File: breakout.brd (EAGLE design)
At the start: 25.4 x 32.4 mm, 20 parts, among them IC2 REG1117, Y1 12mhz

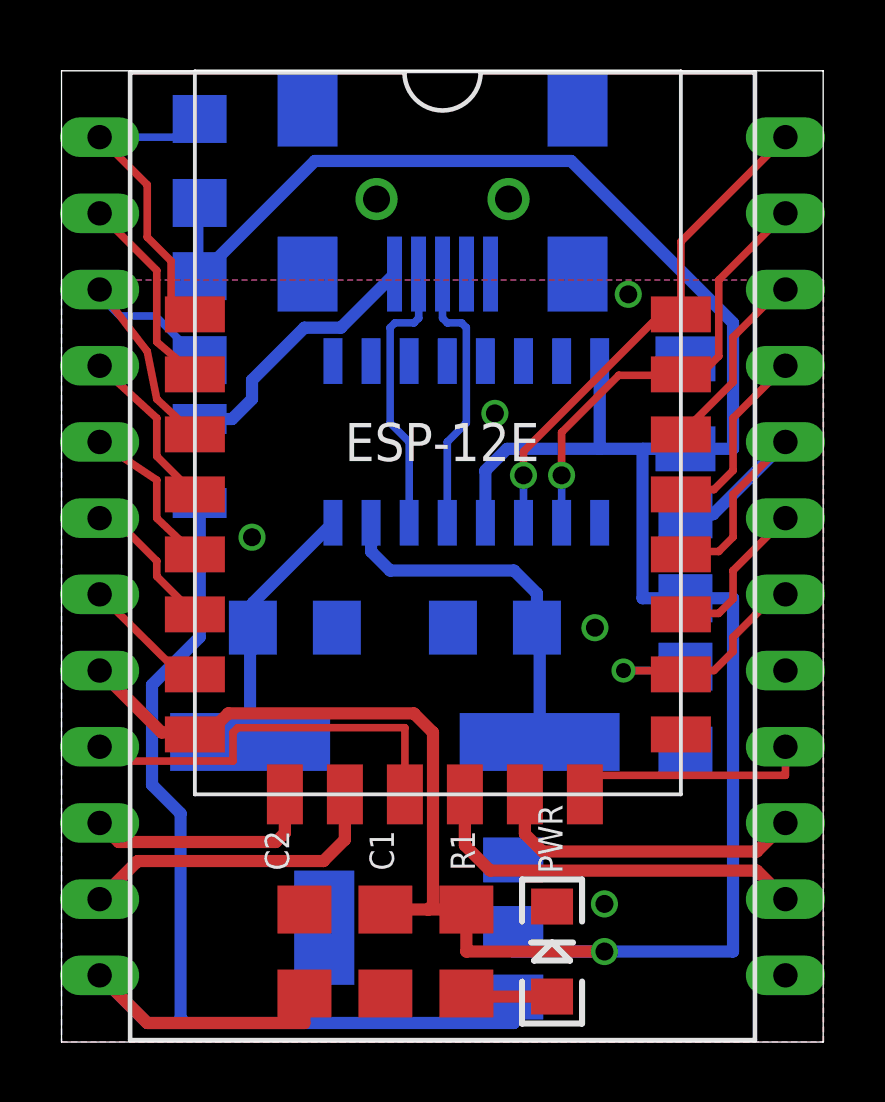
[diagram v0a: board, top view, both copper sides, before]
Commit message: Added a polarised 47uf size B capacitor to the 3.3v rail. Removed thermals from fill layers
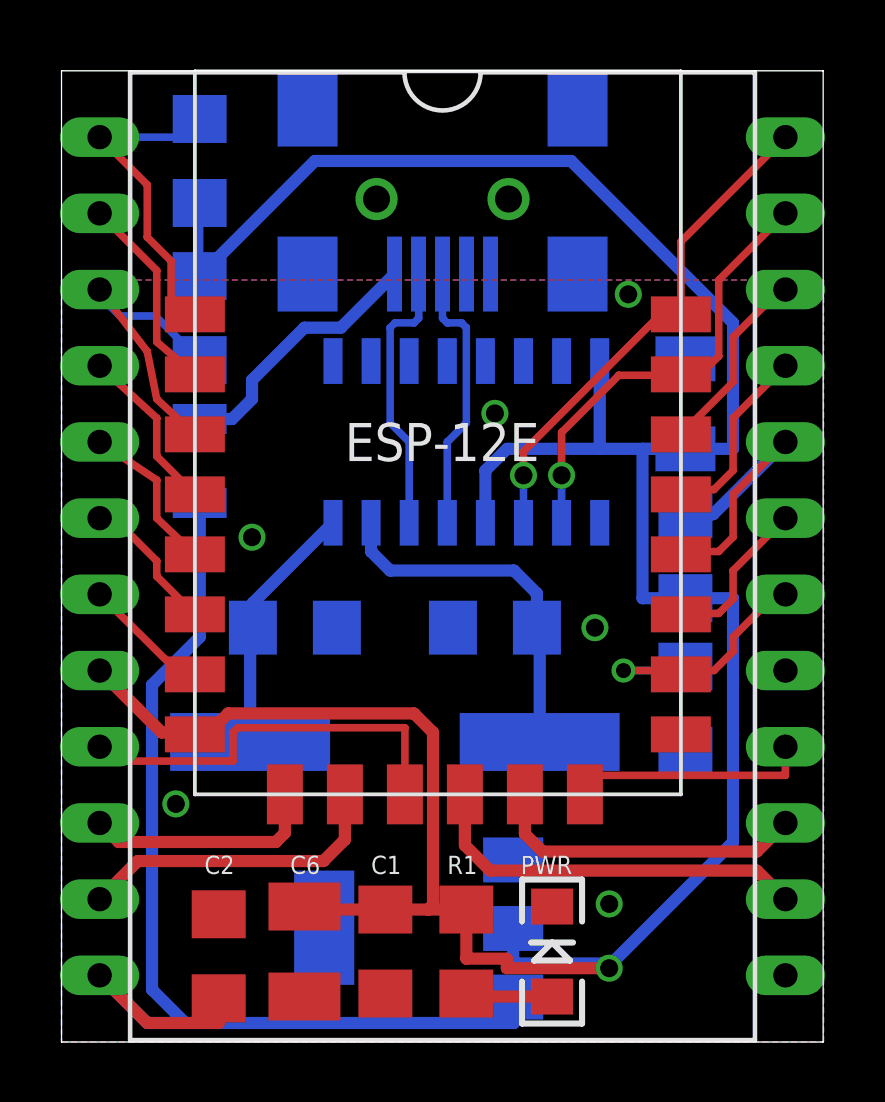
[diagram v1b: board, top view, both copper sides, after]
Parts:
- added C6: 47uf, rcl:SMC_B
- moved C2 2.86 mm to (5.24, 2.86)
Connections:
- net 3.3V: now also C6.+
- net GND: now also C6.-
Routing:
- net 5V: track 42.3 -> 39.2 mm
- net 3.3V: track 99.4 -> 101.6 mm
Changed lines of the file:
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@@
 <?xml version="1.0" encoding="utf-8"?>
 <!DOCTYPE eagle SYSTEM "eagle.dtd">
-<eagle version="7.4.0">
+<eagle version="7.5.0">
 <drawing>
 <settings>
@@
 <setting verticaltext="up"/>
 </settings>
-<grid distance="0.00625" unitdist="inch" unit="mm" style="lines" multiple="1" display="no" altdistance="0.025" altunitdist="inch" altunit="inch"/>
+<grid distance="0.003125" unitdist="inch" unit="inch" style="lines" multiple="1" display="no" altdistance="0.025" altunitdist="inch" altunit="inch"/>
 <layers>
 <layer number="1" name="Top" color="4" fill="1" visible="yes" active="yes"/>
-<layer number="2" name="Route2" color="1" fill="3" visible="no" active="yes"/>
+<layer number="2" name="Route2" color="1" fill="3" visible="yes" active="yes"/>
 <layer number="3" name="Route3" color="4" fill="3" visible="no" active="yes"/>
 <layer number="14" name="Route14" color="1" fill="6" visible="no" active="yes"/>
@@
 <element name="MDL1" library="ESP8266-ESP12E" package="ESP8266-ESP12E" value="" x="4.445" y="8.255" smashed="yes"/>
 <element name="C1" library="SparkFun-Capacitors" package="1206" value="0.1uf" x="10.795" y="3.01625" smashed="yes" rot="R270">
-<attribute name="NAME" x="11.08075" y="5.715" size="0.8128" layer="25" rot="R90"/>
-</element>
-<element name="C2" library="SparkFun-Capacitors" package="1206" value="0.1uf" x="8.09625" y="3.01625" smashed="yes" rot="R90">
-<attribute name="NAME" x="7.58825" y="5.715" size="0.8128" layer="25" rot="R90"/>
+<attribute name="NAME" x="10.31875" y="5.6" size="0.6096" layer="25"/>
+</element>
+<element name="C2" library="SparkFun-Capacitors" package="1206" value="0.1uf" x="5.23875" y="2.8575" smashed="yes" rot="R90">
+<attribute name="NAME" x="4.7625" y="5.6" size="0.6096" layer="25"/>
 </element>
 <element name="IC2" library="burr-brown" package="SOT223" value="REG1117" x="11.90625" y="3.81" smashed="yes" rot="MR270">
@@
 </element>
 <element name="PWR" library="SparkFun-LED" package="LED-1206" value="" x="16.35125" y="3.01625" smashed="yes" rot="R90">
-<attribute name="NAME" x="16.7005" y="5.61975" size="0.8128" layer="25" rot="R90"/>
+<attribute name="NAME" x="15.3035" y="5.6" size="0.6096" layer="25"/>
 <attribute name="VALUE" x="18.12925" y="2.00025" size="0.4064" layer="27" rot="R90"/>
 </element>
 <element name="R1" library="SparkFun-Resistors" package="1206" value="330Ohm" x="13.49375" y="3.01625" smashed="yes" rot="R90">
-<attribute name="NAME" x="13.7795" y="5.715" size="0.8128" layer="25" rot="R90"/>
+<attribute name="NAME" x="12.85875" y="5.6" size="0.6096" layer="25"/>
 </element>
 <element name="R4" library="SparkFun-Resistors" package="1206" value="10k" x="4.60375" y="29.36875" smashed="yes" rot="MR90">
@@
 <element name="C4" library="SparkFun-Capacitors" package="1206" value="22pf" x="14.44625" y="13.81125" rot="MR0"/>
 <element name="C5" library="SparkFun-Capacitors" package="1206" value="22pf" x="7.77875" y="13.81125" rot="MR180"/>
+<element name="C6" library="rcl" package="SMC_B" value="47uf" x="8.09625" y="3.01625" smashed="yes" rot="R270">
+<attribute name="NAME" x="7.62" y="5.6" size="0.6096" layer="25"/>
+<attribute name="VALUE" x="27.6225" y="6.19125" size="1.016" layer="27" rot="R270"/>
+</element>
 </elements>
 <signals>
@@
 <wire x1="2.8575" y1="0.635" x2="1.27" y2="2.2225" width="0.4064" layer="16"/>
 <wire x1="1.27" y1="2.2225" x2="2.8575" y2="0.635" width="0.4064" layer="1"/>
-<wire x1="2.8575" y1="0.635" x2="8.09625" y2="0.635" width="0.4064" layer="1"/>
-<wire x1="8.09625" y1="0.635" x2="8.09625" y2="1.61625" width="0.4064" layer="1"/>
 <wire x1="4.60375" y1="17.9675" x2="4.60375" y2="13.49375" width="0.4064" layer="16"/>
 <wire x1="4.60375" y1="13.49375" x2="3.01625" y2="11.90625" width="0.4064" layer="16"/>
-<wire x1="3.01625" y1="11.90625" x2="3.01625" y2="8.5725" width="0.4064" layer="16"/>
-<wire x1="3.01625" y1="8.5725" x2="3.96875" y2="7.62" width="0.4064" layer="16"/>
-<wire x1="3.96875" y1="7.62" x2="3.96875" y2="0.79375" width="0.4064" layer="16"/>
-<wire x1="3.96875" y1="0.79375" x2="4.1275" y2="0.635" width="0.4064" layer="16"/>
+<wire x1="3.01625" y1="11.90625" x2="3.01625" y2="1.74625" width="0.4064" layer="16"/>
+<wire x1="3.01625" y1="1.74625" x2="4.1275" y2="0.635" width="0.4064" layer="16"/>
+<wire x1="5.23875" y1="1.4575" x2="5.23875" y2="0.635" width="0.4064" layer="1"/>
+<wire x1="5.23875" y1="0.635" x2="2.8575" y2="0.635" width="0.4064" layer="1"/>
 </signal>
 <signal name="GPIO12">
@@
 <wire x1="13.49375" y1="4.41625" x2="12.22375" y2="4.41625" width="0.4064" layer="1"/>
 <wire x1="12.22375" y1="4.41625" x2="10.795" y2="4.41625" width="0.4064" layer="1"/>
-<wire x1="15.05585" y1="3.7846" x2="15.05585" y2="3.01625" width="0.4064" layer="16"/>
-<wire x1="15.05585" y1="3.01625" x2="18.0975" y2="3.01625" width="0.4064" layer="16"/>
-<via x="18.0975" y="3.01625" extent="1-16" drill="0.6" shape="square"/>
-<wire x1="18.0975" y1="3.01625" x2="13.49375" y2="3.01625" width="0.4064" layer="1"/>
-<wire x1="13.49375" y1="3.01625" x2="13.49375" y2="4.41625" width="0.4064" layer="1"/>
+<wire x1="15.05585" y1="3.7846" x2="15.05585" y2="2.619375" width="0.4064" layer="16"/>
+<wire x1="15.05585" y1="2.619375" x2="18.25625" y2="2.619375" width="0.4064" layer="16"/>
+<wire x1="18.25625" y1="2.619375" x2="18.25625" y2="2.460625" width="0.4064" layer="16"/>
+<via x="18.25625" y="2.460625" extent="1-16" drill="0.6" shape="square"/>
+<wire x1="18.25625" y1="2.460625" x2="14.843125" y2="2.460625" width="0.4064" layer="1"/>
+<wire x1="14.843125" y1="2.460625" x2="14.843125" y2="2.778125" width="0.4064" layer="1"/>
+<wire x1="14.843125" y1="2.778125" x2="13.49375" y2="2.778125" width="0.4064" layer="1"/>
+<wire x1="13.49375" y1="2.778125" x2="13.49375" y2="4.41625" width="0.4064" layer="1"/>
 <wire x1="19.3675" y1="14.7925" x2="22.38375" y2="14.7925" width="0.4064" layer="16"/>
-<wire x1="22.38375" y1="14.7925" x2="22.38375" y2="3.01625" width="0.4064" layer="16"/>
-<wire x1="22.38375" y1="3.01625" x2="18.0975" y2="3.01625" width="0.4064" layer="16"/>
+<wire x1="22.38375" y1="14.7925" x2="22.38375" y2="6.6675" width="0.4064" layer="16"/>
 <wire x1="4.445" y1="10.255" x2="4.8575" y2="10.255" width="0.4064" layer="1"/>
 <wire x1="4.8575" y1="10.255" x2="5.55625" y2="10.95375" width="0.4064" layer="1"/>
@@
 <wire x1="12.3825" y1="10.31875" x2="12.3825" y2="4.575" width="0.4064" layer="1"/>
 <wire x1="12.3825" y1="4.575" x2="12.22375" y2="4.41625" width="0.4064" layer="1"/>
+<contactref element="C6" pad="+"/>
+<wire x1="8.09625" y1="4.51625" x2="8.09625" y2="4.41625" width="0.4064" layer="1"/>
+<wire x1="8.09625" y1="4.41625" x2="10.795" y2="4.41625" width="0.4064" layer="1"/>
+<wire x1="18.25625" y1="2.460625" x2="18.25625" y2="2.54" width="0.4064" layer="16"/>
+<wire x1="18.25625" y1="2.54" x2="22.38375" y2="6.6675" width="0.4064" layer="16"/>
 </signal>
 <signal name="GPIO13">
@@
 <contactref element="C1" pad="2"/>
 <contactref element="C2" pad="2"/>
-<polygon width="0.4064" layer="16">
+<polygon width="0.4064" layer="16" thermals="no">
 <vertex x="0" y="0"/>
 <vertex x="25.4" y="0"/>
@@
 <vertex x="0" y="25.4"/>
 </polygon>
-<polygon width="0.4064" layer="1">
+<polygon width="0.4064" layer="1" thermals="no">
 <vertex x="0" y="0"/>
 <vertex x="25.4" y="0"/>
@@
 <contactref element="C5" pad="2"/>
 <via x="18.89125" y="24.92375" extent="1-16" drill="0.6" shape="square"/>
-<via x="18.0975" y="4.60375" extent="1-16" drill="0.6" shape="square"/>
+<via x="18.25625" y="4.60375" extent="1-16" drill="0.6" shape="square"/>
 <via x="6.35" y="16.8275" extent="1-16" drill="0.6" shape="square"/>
 <via x="17.78" y="13.81125" extent="1-16" drill="0.6" shape="square"/>
 <via x="14.44625" y="20.955" extent="1-16" drill="0.6" shape="square"/>
+<contactref element="C6" pad="-"/>
+<via x="3.81" y="7.9375" extent="1-16" drill="0.6" shape="square"/>
 </signal>
 <signal name="GPIO2">

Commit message: Fuck it, 0805 all the things, smaller crystal, rejig everything to solder in a less PITA way.
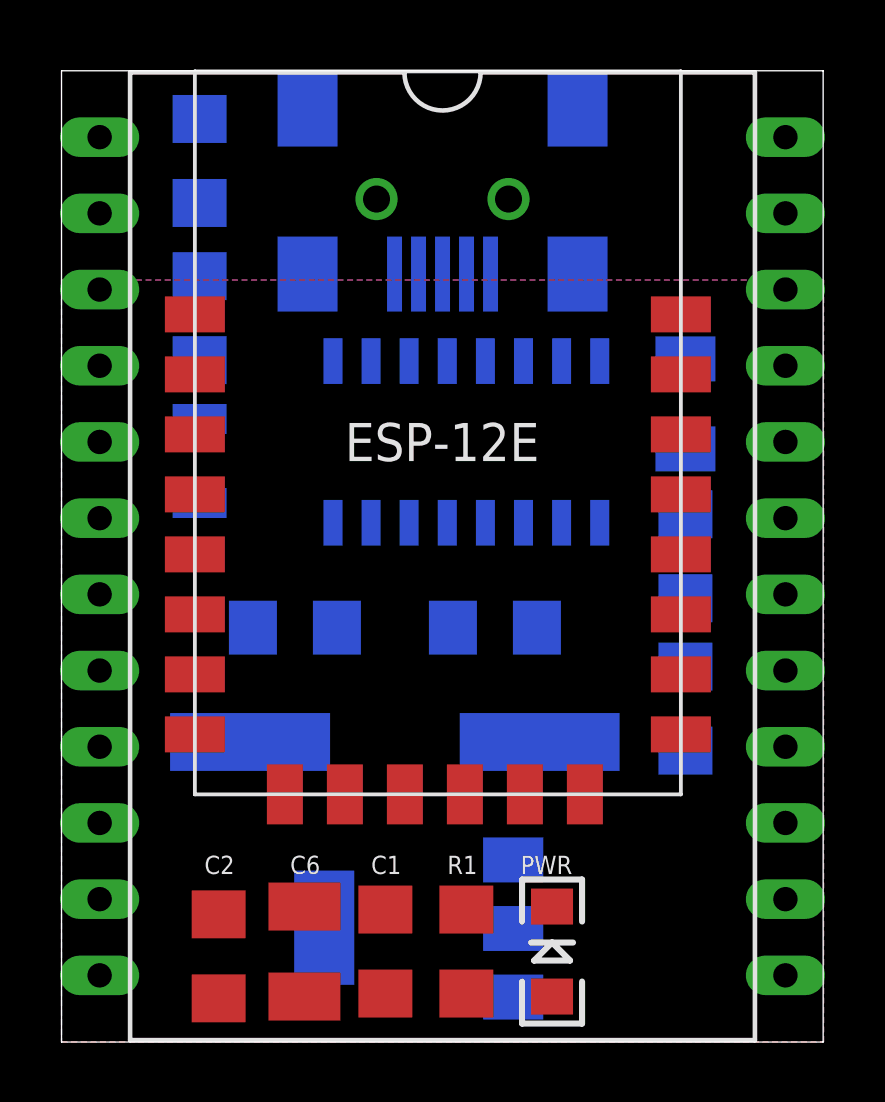
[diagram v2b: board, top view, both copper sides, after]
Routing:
- net 3.3V: track 101.6 -> 0.00 mm, vias 1 -> 0
- net 5V: track 39.2 -> 0.00 mm
- net TX: track 16.9 -> 0.00 mm, vias 1 -> 0
- net RX: track 15.3 -> 0.00 mm, vias 1 -> 0
- net MOSI: track 13.9 -> 0.00 mm
- net SCLK: track 13.1 -> 0.00 mm
- net OSCI: track 12.1 -> 0.00 mm
- net RESET: track 10.9 -> 0.00 mm
- net CS0: track 10.6 -> 0.00 mm
- net GPIO9: track 10.5 -> 0.00 mm
- net CH_PD: track 10.4 -> 0.00 mm
- net GPIO0: track 10.2 -> 0.00 mm
- net USB_D-: track 9.32 -> 0.00 mm
- net USB_D+: track 9.16 -> 0.00 mm
- net GPIO15: track 9.03 -> 0.00 mm, vias 1 -> 0
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
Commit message: Added TX/RX LEDs. Aww yiss.
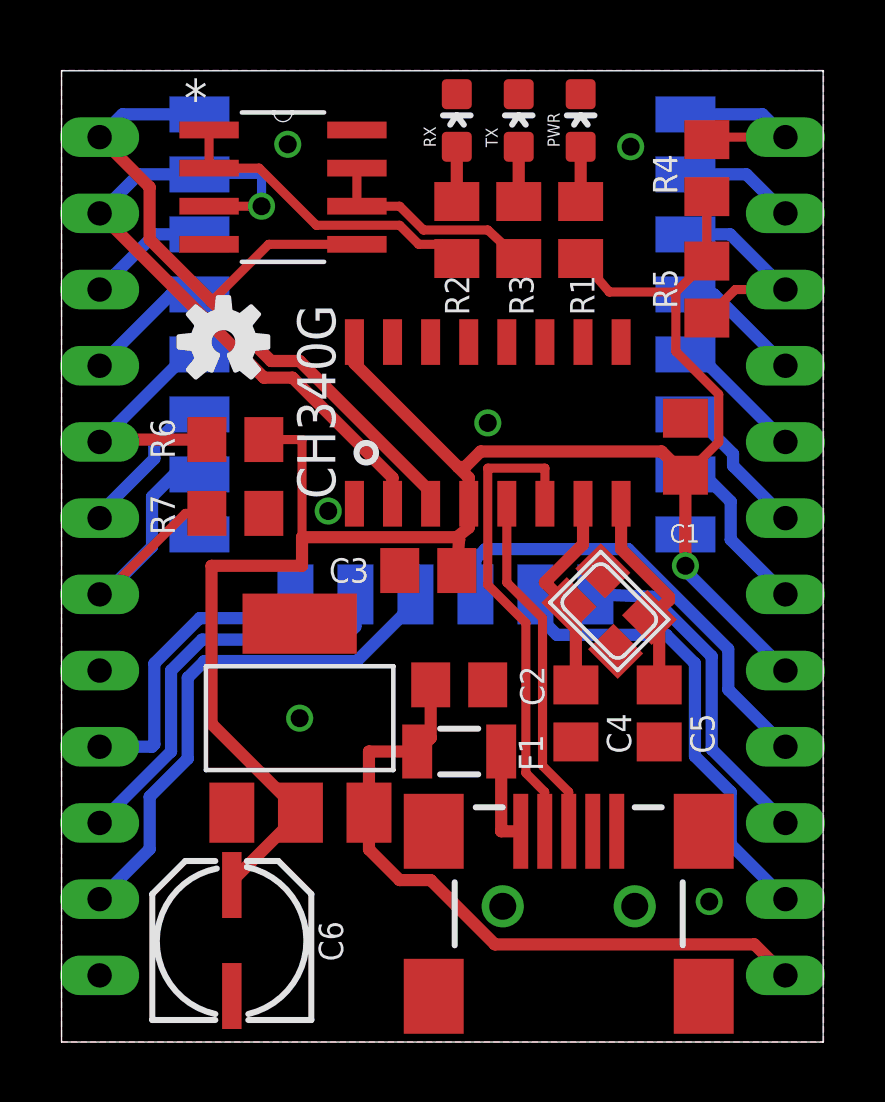
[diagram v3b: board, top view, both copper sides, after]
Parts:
- removed Y1: 12mhz, SparkFun-FreqCtrl:HC49UP
- added Q1: 12Mhz, adafruit:NX3225
- added R2, R3: 330Ohm, rcl:R0805
- added RX, TX: yellow, SparkFun-LED:LED-0603
- added U1: LM358DR, Texas Instruments_By_element14_Batch_1:SOIC127P600X175-8N
- C1, C2, C4, C5: device SparkFun-Capacitors:1206 -> rcl:C0805
- C3: device rcl:C1206K -> rcl:C0805
- C6: device rcl:SMC_B -> SparkFun:PANASONIC_C
- PWR: value (none) -> red; device SparkFun-LED:LED-1206 -> SparkFun-LED:LED-0603
- R1, R4, R5, R6, R7: device SparkFun-Resistors:1206 -> rcl:R0805
- moved PWR 27.7 mm to (17.3, 30.7), turned to 0 degrees
- moved R1 24.4 mm to (17.3, 27.1), turned to 270 degrees
- moved USB 23.9 mm to (16.9, 4.52), flipped to the top, turned to 90 degrees
- moved C1 19.6 mm to (20.8, 19.8), turned to 90 degrees
- moved MDL1 17.7 mm to (20.8, 14.9), flipped to the bottom
- moved R5 16.9 mm to (21.5, 25.1), flipped to the top
- moved R4 16.9 mm to (21.5, 29.1), flipped to the top
- moved LOGO1 16.6 mm to (5.40, 23.3), flipped to the top
- moved R7 16.4 mm to (5.79, 17.6), flipped to the top, turned to 180 degrees
- moved R6 15.5 mm to (5.79, 20.1), flipped to the top, turned to 180 degrees
- moved F1 13.0 mm to (13.3, 9.68), flipped to the top, turned to 180 degrees
- moved C5 12.5 mm to (19.9, 11.0), flipped to the top, turned to 270 degrees
- moved C2 12.1 mm to (13.3, 11.9), turned to 0 degrees
- moved C3 10.2 mm to (12.2, 15.7), flipped to the top, turned to 180 degrees
- moved IC2 8.03 mm to (7.94, 10.8), flipped to the top, turned to 0 degrees
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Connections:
- removed net N$12: U$1.9
- removed net N$13: U$1.10
- removed net N$14: U$1.11
- removed net N$15: U$1.12
- removed net N$16: U$1.13
- removed net N$17: U$1.14
- removed net N$18: U$1.15
- new net N$2: R3.2, TX.A
- new net N$3: R2.1, U1.1, U1.2
- new net N$4: R3.1, U1.6, U1.7
- new net N$5: R2.2, RX.A
- net 3.3V: now also U1.8
- net GND: now also Q1.2, Q1.4, RX.C, TX.C, U1.4
- net OSCI: now also Q1.1; no longer Y1.1
- net OSCO: now also Q1.3; no longer Y1.2
- net RX: now also U1.3
- net TX: now also U1.5
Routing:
- net 3.3V: track 0.00 -> 67.4 mm, vias 0 -> 1
- net TX: track 0.00 -> 26.6 mm
- net RX: track 0.00 -> 23.0 mm, vias 0 -> 1
- net 5V: track 0.00 -> 22.9 mm
- net SCLK: track 0.00 -> 17.5 mm
- net USB_D-: track 0.00 -> 16.0 mm
- net GPIO9: track 0.00 -> 15.8 mm
- net MOSI: track 0.00 -> 15.2 mm
- net CS0: track 0.00 -> 13.9 mm
- net USB_D+: track 0.00 -> 11.8 mm
- net MISO: track 0.00 -> 11.3 mm
- net N$3: track 0.00 -> 10.8 mm
- net GPIO15: track 0.00 -> 10.7 mm
- net GPIO10: track 0.00 -> 10.7 mm
- net GPIO0: track 0.00 -> 8.14 mm
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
